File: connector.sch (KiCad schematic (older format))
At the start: 2 parts

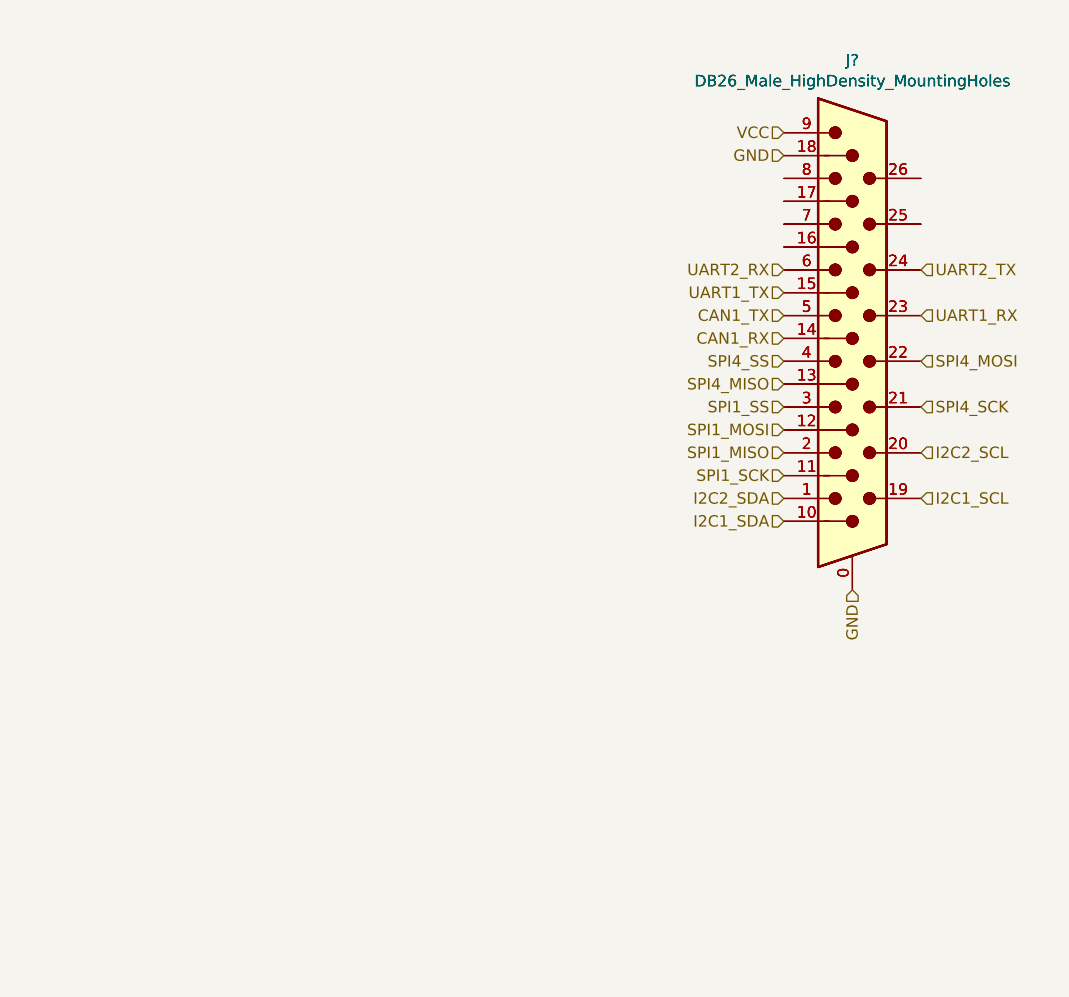
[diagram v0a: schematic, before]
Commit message: create cutout
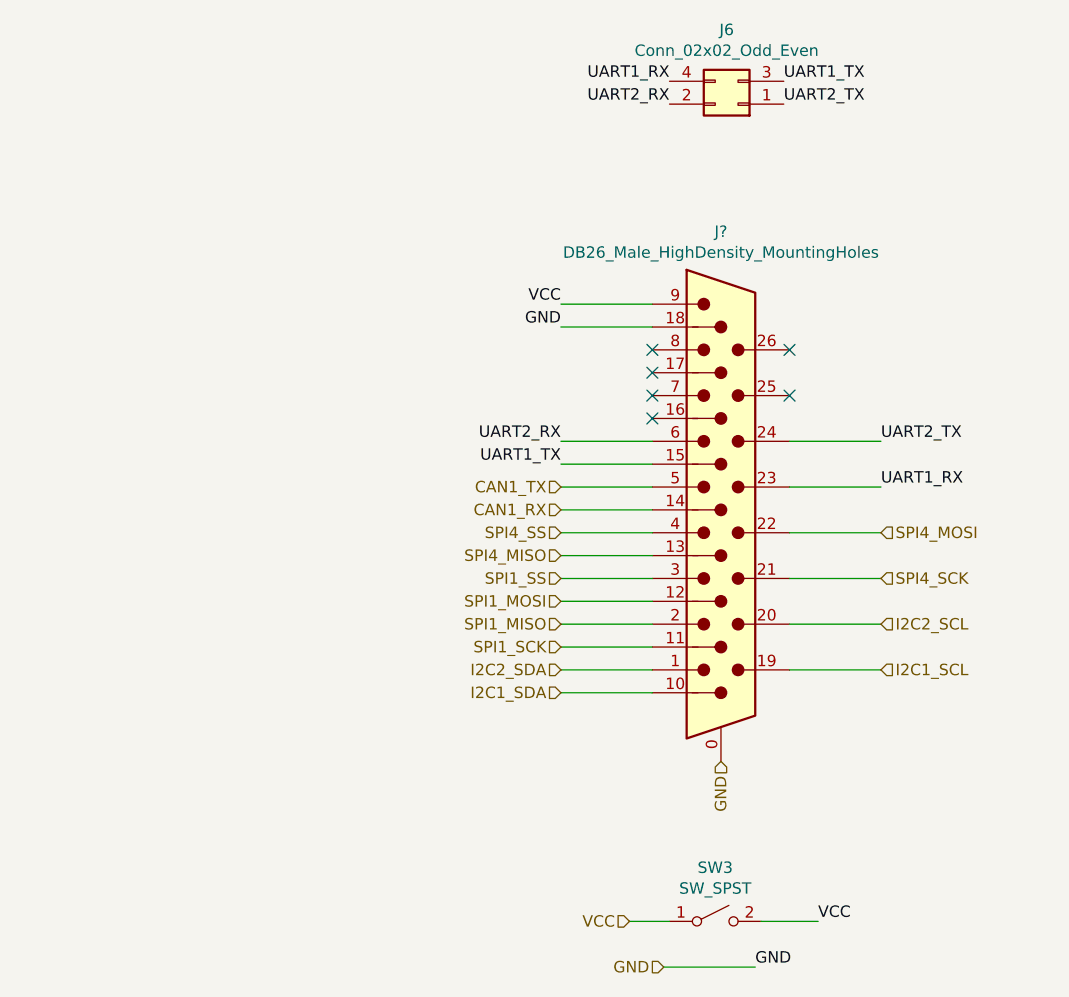
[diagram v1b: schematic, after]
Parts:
- removed J?: DB26_Male_HighDensity_MountingHoles, symbol db26hd:DB26_Male_HighDensity_MountingHoles
- added J6: Conn_02x02_Odd_Even, symbol Connector_Generic:Conn_02x02_Odd_Even
- added SW3: SW_SPST, symbol Switch:SW_SPST
- J1: renamed from J?; footprint (none) -> Connector_Dsub:DSUB-26-HD_Male_Horizontal_P2.29x1.98mm_EdgePinOffset3.03mm_Housed_MountingHolesOffset4.94mm
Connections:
- net UART1_RX: now also J6.4 (Pin_4)
- net UART1_TX: now also J6.3 (Pin_3)
- net UART2_RX: now also J6.2 (Pin_2)
- net UART2_TX: now also J6.1 (Pin_1)
- net VCC: now also SW3.1 (A), SW3.2 (B)
- no-connect marks 0 -> 6
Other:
- moved on the sheet: J?

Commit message: schematic improvements
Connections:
- net VCC: no longer J1.9, SW3.2 (B)
- new net: J1.9, SW3.2 (B)
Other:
- moved on the sheet: SW3
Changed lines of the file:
@@
 Text HLabel 4725 5000 0    50   Input ~ 0
 I2C1_SDA
-Text HLabel 5425 5300 3    50   Input ~ 0
-GND
 Text HLabel 6125 4900 2    50   Input ~ 0
 I2C1_SCL
@@
 Text HLabel 6125 4300 2    50   Input ~ 0
 SPI4_MOSI
-Text HLabel 5025 6000 0    50   Input ~ 0
-VCC
-Text HLabel 5175 6200 0    50   Input ~ 0
-GND
 Text HLabel 4725 4500 0    50   Input ~ 0
 SPI1_SS
@@
 L Switch:SW_SPST SW3
 U 1 1 5F134DBC
-P 5400 6000
+P 4675 3300
 AR Path="/5F06A0A3/5F134DBC" Ref="SW3"  Part="1"
 AR Path="/5F152747/5F134DBC" Ref="SW1"  Part="1"
@@
 AR Path="/5F1649A2/5F134DBC" Ref="SW?"  Part="1"
 AR Path="/5F1649C4/5F134DBC" Ref="SW?"  Part="1"
-F 0 "SW?" H 5400 6235 50  0000 C CNN
-F 1 "SW_SPST" H 5400 6144 50  0000 C CNN
-F 2 "" H 5400 6000 50  0001 C CNN
-F 3 "~" H 5400 6000 50  0001 C CNN
-	1    5400 6000
-	1    0    0    -1
-$EndComp
-Wire Wire Line
-	5200 6000 5025 6000
-Wire Wire Line
-	5600 6000 5850 6000
+F 0 "SW?" H 4675 3535 50  0000 C CNN
+F 1 "SW_SPST" H 4675 3444 50  0000 C CNN
+F 2 "" H 4675 3300 50  0001 C CNN
+F 3 "~" H 4675 3300 50  0001 C CNN
+	1    4675 3300
+	1    0    0    -1
+$EndComp
+Wire Wire Line
+	4475 3300 4300 3300
+Wire Wire Line
+	4875 3300 5125 3300
 $Comp
 L Connector_Generic:Conn_02x02_Odd_Even J6
@@
 UART2_TX
 Wire Wire Line
-	5575 6200 5175 6200
-Text Label 5575 6200 0    50   ~ 0
-GND
-Text Label 5850 6000 0    50   ~ 0
-VCC
-Text Label 4725 3300 2    50   ~ 0
-VCC
-Text Label 4725 3400 2    50   ~ 0
-GND
-Wire Wire Line
-	5125 3300 4725 3300
-Wire Wire Line
 	5125 3400 4725 3400
+$Comp
+L power:VCC #PWR?
+U 1 1 5F4B6D92
+P 4300 3300
+F 0 "#PWR?" H 4300 3150 50  0001 C CNN
+F 1 "VCC" H 4317 3473 50  0000 C CNN
+F 2 "" H 4300 3300 50  0001 C CNN
+F 3 "" H 4300 3300 50  0001 C CNN
+	1    4300 3300
+	1    0    0    -1
+$EndComp
+$Comp
+L power:GND #PWR?
+U 1 1 5F4B7169
+P 4725 3400
+F 0 "#PWR?" H 4725 3150 50  0001 C CNN
+F 1 "GND" H 4730 3227 50  0000 C CNN
+F 2 "" H 4725 3400 50  0001 C CNN
+F 3 "" H 4725 3400 50  0001 C CNN
+	1    4725 3400
+	1    0    0    -1
+$EndComp
+$Comp
+L power:GND #PWR?
+U 1 1 5F4B88F0
+P 5425 5300
+F 0 "#PWR?" H 5425 5050 50  0001 C CNN
+F 1 "GND" H 5430 5127 50  0000 C CNN
+F 2 "" H 5425 5300 50  0001 C CNN
+F 3 "" H 5425 5300 50  0001 C CNN
+	1    5425 5300
+	1    0    0    -1
+$EndComp
 $EndSCHEMATC

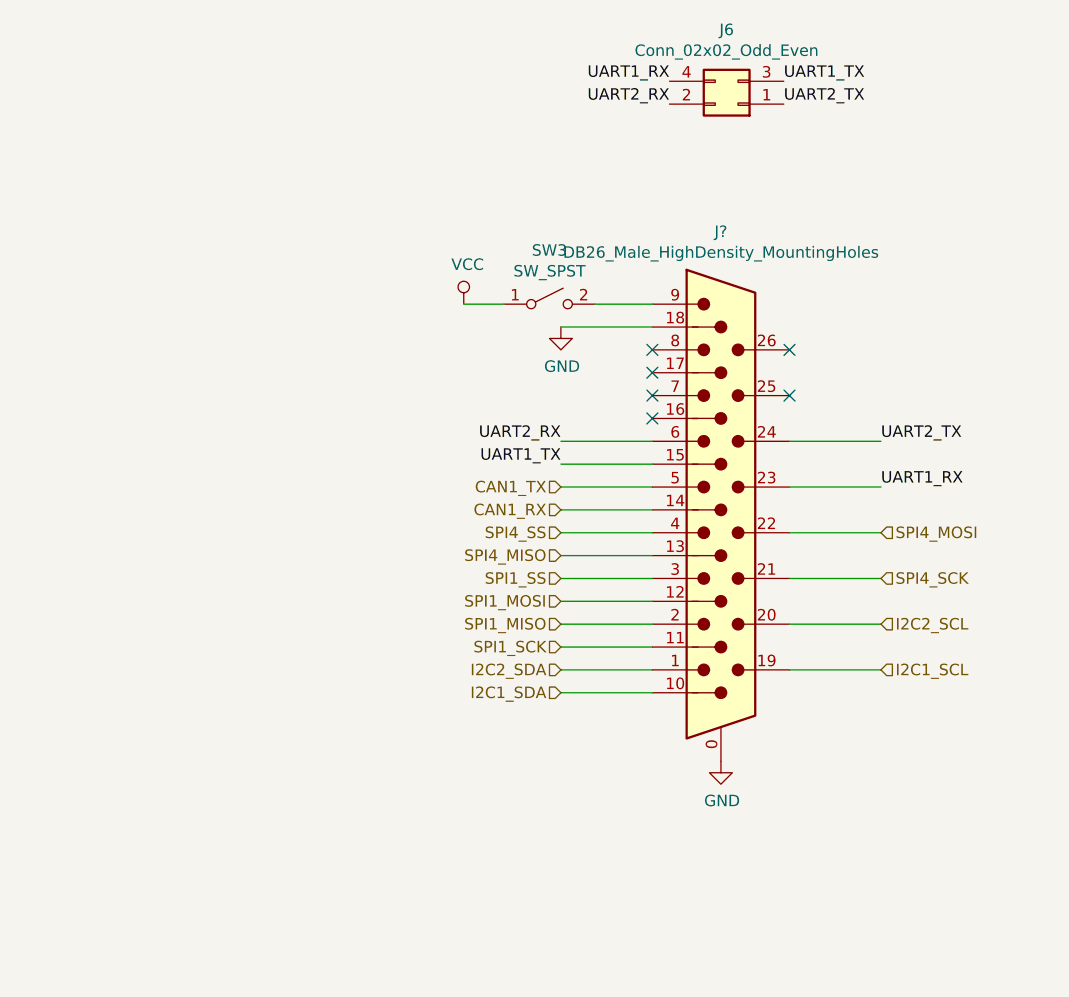
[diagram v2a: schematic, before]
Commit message: add power management wiring and mounting holes
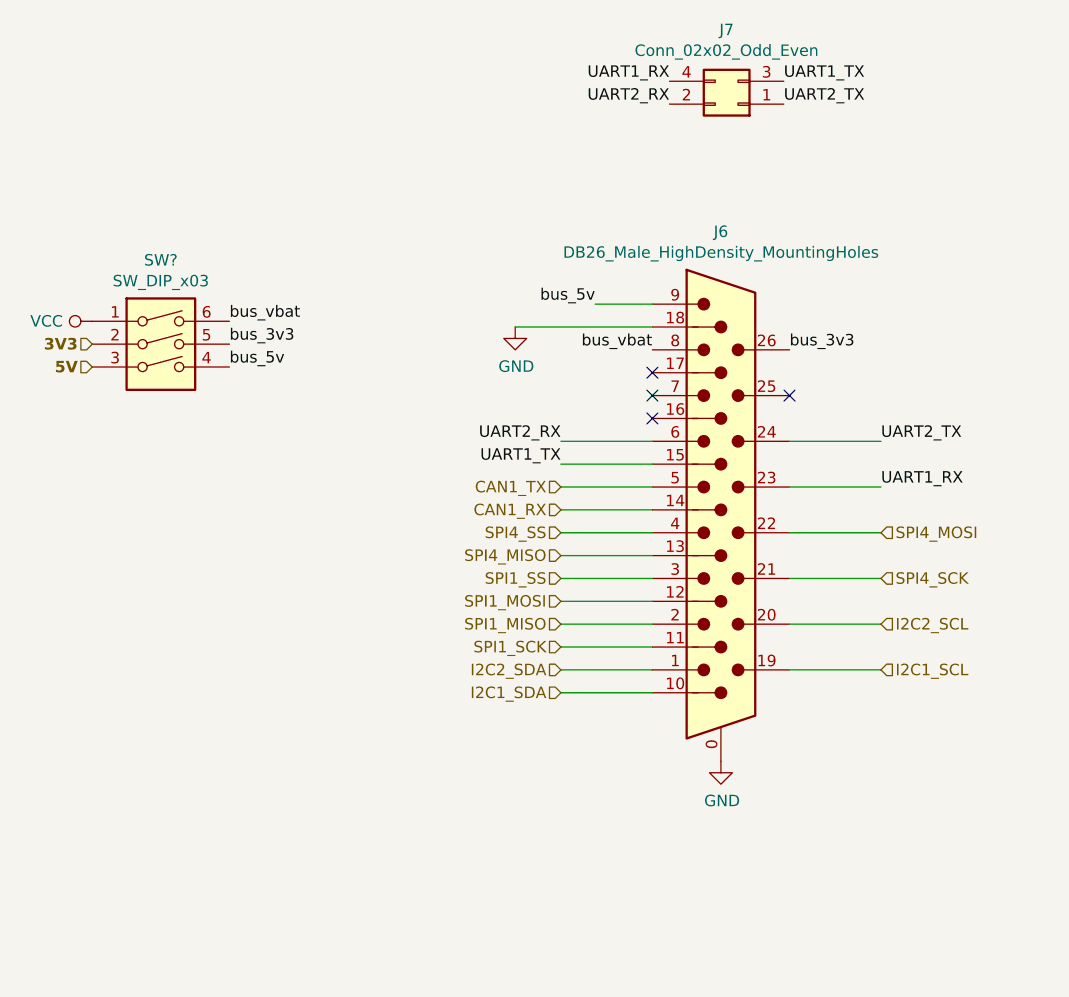
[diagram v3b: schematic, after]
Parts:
- removed SW3: SW_SPST, symbol Switch:SW_SPST
- added SW?: SW_DIP_x03, symbol Switch:SW_DIP_x03
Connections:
- net VCC: now also SW?.1
- net bus_5v: now reaches J1.9
- net bus_5v: now also SW?.4
- net bus_3v3: now reaches J1.26
- net bus_3v3: now also SW?.5
- net bus_vbat: now reaches J1.8
- net bus_vbat: now also SW?.6
- new net 3V3: SW?.2
- new net 5V: SW?.3
- no-connect marks 6 -> 4
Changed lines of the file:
@@
 $Descr A4 11693 8268
 encoding utf-8
-Sheet 2 2
+Sheet 7 17
 Title ""
 Date ""
@@
 AR Path="/5F1649A2/5F14DCB5" Ref="J?"  Part="1"
 AR Path="/5F1649C4/5F14DCB5" Ref="J?"  Part="1"
-F 0 "J?" H 5425 6217 50  0000 C CNN
+AR Path="/5F10DACE/5F10EEE2/5F14DCB5" Ref="J2"  Part="1"
+AR Path="/5F1100AF/5F10EEE2/5F14DCB5" Ref="J?"  Part="1"
+AR Path="/5F1100FD/5F10EEE2/5F14DCB5" Ref="J?"  Part="1"
+AR Path="/5F110145/5F10EEE2/5F14DCB5" Ref="J?"  Part="1"
+AR Path="/5F11031E/5F10EEE2/5F14DCB5" Ref="J?"  Part="1"
+AR Path="/5F110320/5F10EEE2/5F14DCB5" Ref="J?"  Part="1"
+AR Path="/5F110322/5F10EEE2/5F14DCB5" Ref="J?"  Part="1"
+AR Path="/5F110324/5F10EEE2/5F14DCB5" Ref="J?"  Part="1"
+AR Path="/5F1123F9/5F10EEE2/5F14DCB5" Ref="J4"  Part="1"
+AR Path="/5F11264C/5F10EEE2/5F14DCB5" Ref="J6"  Part="1"
+AR Path="/5F11264F/5F10EEE2/5F14DCB5" Ref="J8"  Part="1"
+AR Path="/5F11285A/5F10EEE2/5F14DCB5" Ref="J10"  Part="1"
+AR Path="/5F11285D/5F10EEE2/5F14DCB5" Ref="J12"  Part="1"
+AR Path="/5F112860/5F10EEE2/5F14DCB5" Ref="J14"  Part="1"
+AR Path="/5F112863/5F10EEE2/5F14DCB5" Ref="J16"  Part="1"
+F 0 "J6" H 5425 6217 50  0000 C CNN
 F 1 "DB26_Male_HighDensity_MountingHoles" H 5425 6126 50  0000 C CNN
 F 2 "Connector_Dsub:DSUB-26-HD_Male_Horizontal_P2.29x1.98mm_EdgePinOffset3.03mm_Housed_MountingHolesOffset4.94mm" H 4475 5000 50  0001 C CNN
@@
 	1    0    0    -1
 $EndComp
-NoConn ~ 5725 3500
 NoConn ~ 5725 3700
-NoConn ~ 5125 3500
 NoConn ~ 5125 3600
 NoConn ~ 5125 3700
 NoConn ~ 5125 3800
-$Comp
-L Switch:SW_SPST SW3
-U 1 1 5F134DBC
-P 4675 3300
-AR Path="/5F06A0A3/5F134DBC" Ref="SW3"  Part="1"
-AR Path="/5F152747/5F134DBC" Ref="SW1"  Part="1"
-AR Path="/5F055BCC/5F134DBC" Ref="SW2"  Part="1"
-AR Path="/5F06A0CD/5F134DBC" Ref="SW4"  Part="1"
-AR Path="/5F08D74B/5F134DBC" Ref="SW5"  Part="1"
-AR Path="/5F08D775/5F134DBC" Ref="SW6"  Part="1"
-AR Path="/5F08D79F/5F134DBC" Ref="SW7"  Part="1"
-AR Path="/5F08D7C9/5F134DBC" Ref="SW8"  Part="1"
-AR Path="/5F15D051/5F134DBC" Ref="SW4"  Part="1"
-AR Path="/5F1620BA/5F134DBC" Ref="SW?"  Part="1"
-AR Path="/5F162B2E/5F134DBC" Ref="SW?"  Part="1"
-AR Path="/5F162B50/5F134DBC" Ref="SW?"  Part="1"
-AR Path="/5F16495E/5F134DBC" Ref="SW?"  Part="1"
-AR Path="/5F164980/5F134DBC" Ref="SW?"  Part="1"
-AR Path="/5F1649A2/5F134DBC" Ref="SW?"  Part="1"
-AR Path="/5F1649C4/5F134DBC" Ref="SW?"  Part="1"
-F 0 "SW?" H 4675 3535 50  0000 C CNN
-F 1 "SW_SPST" H 4675 3444 50  0000 C CNN
-F 2 "" H 4675 3300 50  0001 C CNN
-F 3 "~" H 4675 3300 50  0001 C CNN
-	1    4675 3300
-	1    0    0    -1
-$EndComp
-Wire Wire Line
-	4475 3300 4300 3300
 Wire Wire Line
 	4875 3300 5125 3300
@@
 AR Path="/5F1649A2/5F139BC3" Ref="J?"  Part="1"
 AR Path="/5F1649C4/5F139BC3" Ref="J?"  Part="1"
-F 0 "J?" H 5550 2100 50  0000 C CNN
+AR Path="/5F10DACE/5F10EEE2/5F139BC3" Ref="J3"  Part="1"
+AR Path="/5F1100AF/5F10EEE2/5F139BC3" Ref="J?"  Part="1"
+AR Path="/5F1100FD/5F10EEE2/5F139BC3" Ref="J?"  Part="1"
+AR Path="/5F110145/5F10EEE2/5F139BC3" Ref="J?"  Part="1"
+AR Path="/5F11031E/5F10EEE2/5F139BC3" Ref="J?"  Part="1"
+AR Path="/5F110320/5F10EEE2/5F139BC3" Ref="J?"  Part="1"
+AR Path="/5F110322/5F10EEE2/5F139BC3" Ref="J?"  Part="1"
+AR Path="/5F110324/5F10EEE2/5F139BC3" Ref="J?"  Part="1"
+AR Path="/5F1123F9/5F10EEE2/5F139BC3" Ref="J5"  Part="1"
+AR Path="/5F11264C/5F10EEE2/5F139BC3" Ref="J7"  Part="1"
+AR Path="/5F11264F/5F10EEE2/5F139BC3" Ref="J9"  Part="1"
+AR Path="/5F11285A/5F10EEE2/5F139BC3" Ref="J11"  Part="1"
+AR Path="/5F11285D/5F10EEE2/5F139BC3" Ref="J13"  Part="1"
+AR Path="/5F112860/5F10EEE2/5F139BC3" Ref="J15"  Part="1"
+AR Path="/5F112863/5F10EEE2/5F139BC3" Ref="J17"  Part="1"
+F 0 "J7" H 5550 2100 50  0000 C CNN
 F 1 "Conn_02x02_Odd_Even" H 5550 2191 50  0000 C CNN
 F 2 "" H 5500 2425 50  0001 C CNN
@@
 UART2_TX
 Wire Wire Line
-	5125 3400 4725 3400
-$Comp
-L power:VCC #PWR?
-U 1 1 5F4B6D92
-P 4300 3300
-F 0 "#PWR?" H 4300 3150 50  0001 C CNN
-F 1 "VCC" H 4317 3473 50  0000 C CNN
-F 2 "" H 4300 3300 50  0001 C CNN
-F 3 "" H 4300 3300 50  0001 C CNN
-	1    4300 3300
+	5125 3400 4525 3400
+$Comp
+L power:GND #PWR013
+U 1 1 5F4B7169
+P 4525 3400
+AR Path="/5F10DACE/5F10EEE2/5F4B7169" Ref="#PWR013"  Part="1"
+AR Path="/5F1100AF/5F10EEE2/5F4B7169" Ref="#PWR?"  Part="1"
+AR Path="/5F1100FD/5F10EEE2/5F4B7169" Ref="#PWR?"  Part="1"
+AR Path="/5F110145/5F10EEE2/5F4B7169" Ref="#PWR?"  Part="1"
+AR Path="/5F11031E/5F10EEE2/5F4B7169" Ref="#PWR?"  Part="1"
+AR Path="/5F110320/5F10EEE2/5F4B7169" Ref="#PWR?"  Part="1"
+AR Path="/5F110322/5F10EEE2/5F4B7169" Ref="#PWR?"  Part="1"
+AR Path="/5F110324/5F10EEE2/5F4B7169" Ref="#PWR?"  Part="1"
+AR Path="/5F1123F9/5F10EEE2/5F4B7169" Ref="#PWR016"  Part="1"
+AR Path="/5F11264C/5F10EEE2/5F4B7169" Ref="#PWR019"  Part="1"
+AR Path="/5F11264F/5F10EEE2/5F4B7169" Ref="#PWR022"  Part="1"
+AR Path="/5F11285A/5F10EEE2/5F4B7169" Ref="#PWR025"  Part="1"
+AR Path="/5F11285D/5F10EEE2/5F4B7169" Ref="#PWR028"  Part="1"
+AR Path="/5F112860/5F10EEE2/5F4B7169" Ref="#PWR031"  Part="1"
+AR Path="/5F112863/5F10EEE2/5F4B7169" Ref="#PWR034"  Part="1"
+F 0 "#PWR019" H 4525 3150 50  0001 C CNN
+F 1 "GND" H 4530 3227 50  0000 C CNN
+F 2 "" H 4525 3400 50  0001 C CNN
+F 3 "" H 4525 3400 50  0001 C CNN
+	1    4525 3400
 	1    0    0    -1
 $EndComp
 $Comp
-L power:GND #PWR?
-U 1 1 5F4B7169
-P 4725 3400
-F 0 "#PWR?" H 4725 3150 50  0001 C CNN
-F 1 "GND" H 4730 3227 50  0000 C CNN
-F 2 "" H 4725 3400 50  0001 C CNN
-F 3 "" H 4725 3400 50  0001 C CNN
-	1    4725 3400
-	1    0    0    -1
-$EndComp
-$Comp
-L power:GND #PWR?
+L power:GND #PWR014
 U 1 1 5F4B88F0
 P 5425 5300
-F 0 "#PWR?" H 5425 5050 50  0001 C CNN
+AR Path="/5F10DACE/5F10EEE2/5F4B88F0" Ref="#PWR014"  Part="1"
+AR Path="/5F1100AF/5F10EEE2/5F4B88F0" Ref="#PWR?"  Part="1"
+AR Path="/5F1100FD/5F10EEE2/5F4B88F0" Ref="#PWR?"  Part="1"
+AR Path="/5F110145/5F10EEE2/5F4B88F0" Ref="#PWR?"  Part="1"
+AR Path="/5F11031E/5F10EEE2/5F4B88F0" Ref="#PWR?"  Part="1"
+AR Path="/5F110320/5F10EEE2/5F4B88F0" Ref="#PWR?"  Part="1"
+AR Path="/5F110322/5F10EEE2/5F4B88F0" Ref="#PWR?"  Part="1"
+AR Path="/5F110324/5F10EEE2/5F4B88F0" Ref="#PWR?"  Part="1"
+AR Path="/5F1123F9/5F10EEE2/5F4B88F0" Ref="#PWR017"  Part="1"
+AR Path="/5F11264C/5F10EEE2/5F4B88F0" Ref="#PWR020"  Part="1"
+AR Path="/5F11264F/5F10EEE2/5F4B88F0" Ref="#PWR023"  Part="1"
+AR Path="/5F11285A/5F10EEE2/5F4B88F0" Ref="#PWR026"  Part="1"
+AR Path="/5F11285D/5F10EEE2/5F4B88F0" Ref="#PWR029"  Part="1"
+AR Path="/5F112860/5F10EEE2/5F4B88F0" Ref="#PWR032"  Part="1"
+AR Path="/5F112863/5F10EEE2/5F4B88F0" Ref="#PWR035"  Part="1"
+F 0 "#PWR020" H 5425 5050 50  0001 C CNN
 F 1 "GND" H 5430 5127 50  0000 C CNN
 F 2 "" H 5425 5300 50  0001 C CNN
@@
 	1    0    0    -1
 $EndComp
+Text HLabel 2675 3475 0    50   Input ~ 10
+3V3
+Text HLabel 2675 3575 0    50   Input ~ 10
+5V
+$Comp
+L Switch:SW_DIP_x03 SW?
+U 1 1 5F14E492
+P 2975 3575
+AR Path="/5F1123F9/5F10EEE2/5F14E492" Ref="SW?"  Part="1"
+AR Path="/5F11264C/5F10EEE2/5F14E492" Ref="SW?"  Part="1"
+F 0 "SW?" H 2975 4042 50  0000 C CNN
+F 1 "SW_DIP_x03" H 2975 3951 50  0000 C CNN
+F 2 "" H 2975 3575 50  0001 C CNN
+F 3 "~" H 2975 3575 50  0001 C CNN
+	1    2975 3575
+	1    0    0    -1
+$EndComp
+$Comp
+L power:VCC #PWR012
+U 1 1 5F4B6D92
+P 2675 3375
+AR Path="/5F10DACE/5F10EEE2/5F4B6D92" Ref="#PWR012"  Part="1"
+AR Path="/5F1100AF/5F10EEE2/5F4B6D92" Ref="#PWR?"  Part="1"
+AR Path="/5F1100FD/5F10EEE2/5F4B6D92" Ref="#PWR?"  Part="1"
+AR Path="/5F110145/5F10EEE2/5F4B6D92" Ref="#PWR?"  Part="1"
+AR Path="/5F11031E/5F10EEE2/5F4B6D92" Ref="#PWR?"  Part="1"
+AR Path="/5F110320/5F10EEE2/5F4B6D92" Ref="#PWR?"  Part="1"
+AR Path="/5F110322/5F10EEE2/5F4B6D92" Ref="#PWR?"  Part="1"
+AR Path="/5F110324/5F10EEE2/5F4B6D92" Ref="#PWR?"  Part="1"
+AR Path="/5F1123F9/5F10EEE2/5F4B6D92" Ref="#PWR015"  Part="1"
+AR Path="/5F11264C/5F10EEE2/5F4B6D92" Ref="#PWR018"  Part="1"
+AR Path="/5F11264F/5F10EEE2/5F4B6D92" Ref="#PWR021"  Part="1"
+AR Path="/5F11285A/5F10EEE2/5F4B6D92" Ref="#PWR024"  Part="1"
+AR Path="/5F11285D/5F10EEE2/5F4B6D92" Ref="#PWR027"  Part="1"
+AR Path="/5F112860/5F10EEE2/5F4B6D92" Ref="#PWR030"  Part="1"
+AR Path="/5F112863/5F10EEE2/5F4B6D92" Ref="#PWR033"  Part="1"
+F 0 "#PWR018" H 2675 3225 50  0001 C CNN
+F 1 "VCC" V 2675 3575 50  0000 C CNN
+F 2 "" H 2675 3375 50  0001 C CNN
+F 3 "" H 2675 3375 50  0001 C CNN
+	1    2675 3375
+	0    -1   -1   0
+$EndComp
+Text Label 3275 3375 0    50   ~ 0
+bus_vbat
+Text Label 3275 3475 0    50   ~ 0
+bus_3v3
+Text Label 3275 3575 0    50   ~ 0
+bus_5v
+Text Label 4875 3300 2    50   ~ 0
+bus_5v
+Text Label 5125 3500 2    50   ~ 0
+bus_vbat
+Text Label 5725 3500 0    50   ~ 0
+bus_3v3
 $EndSCHEMATC
